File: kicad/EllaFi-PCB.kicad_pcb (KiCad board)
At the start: 2 copper layers, 43.8 x 97.2 mm, 27 parts, among them J1 Conn_01x04_Socket, J2 Conn_01x03, J3 PJ-102AH, J4 Conn_01x22_Socket, J5 Conn_01x22_Socket, Q1 AOD4184A, SW1 2W/3W jumper, U1 FOD817S, U2 ESP32-S3-DevKitC, U3 LM2596S-5

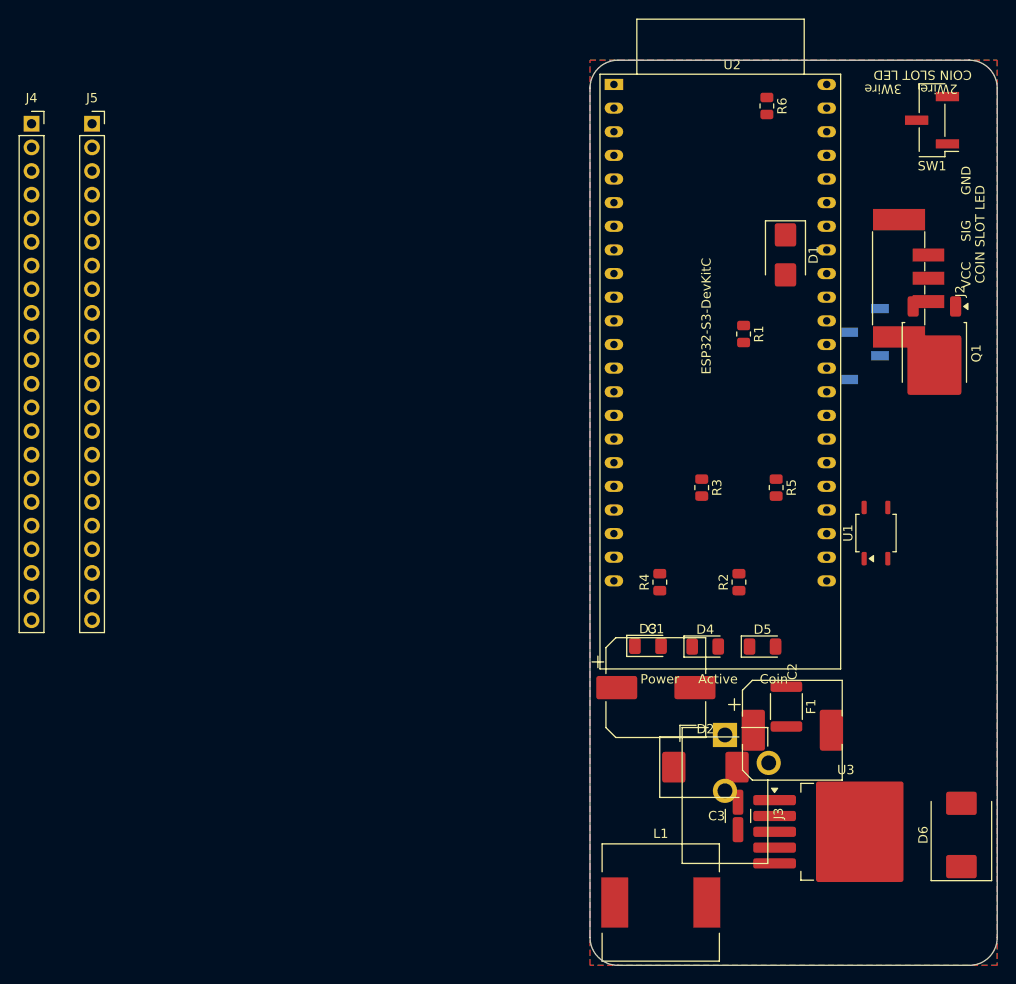
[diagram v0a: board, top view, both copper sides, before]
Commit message: kicad: PCB fully routed + DRC-clean (buck complete)
MPM3620A buck routed (FB on top layer, no via; grounds via'd to the plane), J3/F1/D6 input front-end, coin/signal nets, GND pours filled. Net-class track widths 0.25mm. DRC: 0 unconnected, 0 violations. Buck spike test passes (12.1V vs LM2596's 30.3V).

Co-Authored-By: Claude Opus 4.8 <noreply@anthropic.com>
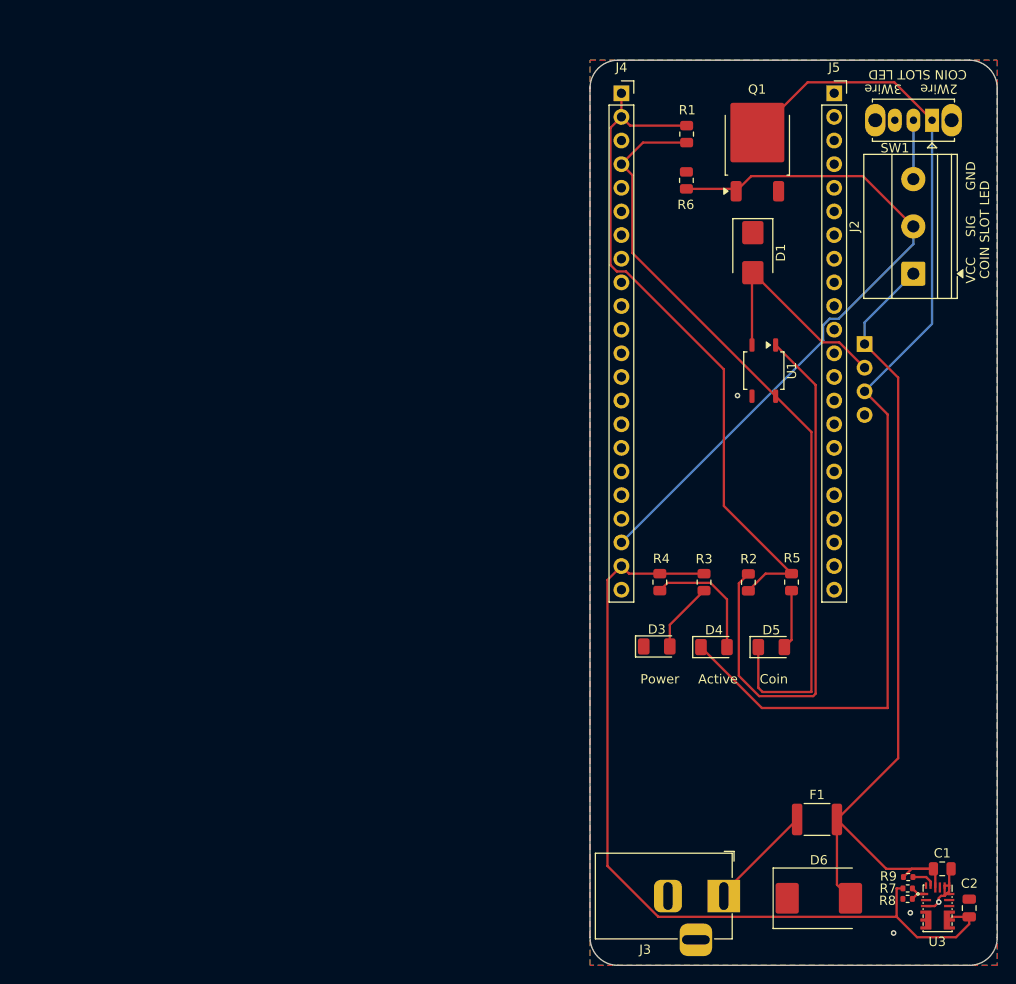
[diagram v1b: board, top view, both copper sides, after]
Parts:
- removed C3: 10uF, Capacitor_SMD:C_1210_3225Metric
- removed D2: SS54, Diode_SMD:D_SMC
- removed L1: 47uH, Inductor_SMD:L_12x12mm_H8mm
- removed U2: ESP32-S3-DevKitC, PCM_Espressif:ESP32-S3-DevKitC
- added R7: 100 kΩ, Resistor_SMD:R_0402_1005Metric, F.Cu at (132.1, 139.5)
- added R8: 19.1 kΩ, Resistor_SMD:R_0402_1005Metric, F.Cu at (132.1, 140.6)
- added R9: 100 kΩ, Resistor_SMD:R_0402_1005Metric, F.Cu at (132.2, 138.3)
- C1: value 220uF 25V -> 10 µF; footprint Capacitor_SMD:CP_Elec_10x10.5 -> Capacitor_SMD:C_0805_2012Metric
- C2: value 220uF 25V -> 22 µF; footprint Capacitor_SMD:CP_Elec_10x10.5 -> Capacitor_SMD:C_0805_2012Metric
- D3: value LED-RED -> RED
- D4: value LED-YELLOW -> YELLOW
- D5: value LED-GREEN -> GREEN
- J1: footprint Connector_PinSocket_2.54mm:PinSocket_1x04_P2.54mm_Vertical_SMD_Pin1Left -> Connector_PinSocket_2.54mm:PinSocket_1x04_P2.54mm_Vertical
- J2: footprint TerminalBlock_Phoenix:TerminalBlock_Phoenix_PTSM-0,5-3-2,5-V-SMD_1x03-1MP_P2.50mm_Vertical -> TerminalBlock_Phoenix:TerminalBlock_Phoenix_MKDS-1,5-3-5.08_1x03_P5.08mm_Horizontal
- J3: value PJ-102AH -> PJ-002AH; footprint Connector_BarrelJack:BarrelJack_CUI_PJ-102AH_Horizontal -> Connector_BarrelJack:BarrelJack_Horizontal
- SW1: value 2W/3W jumper -> OS102011MS2QN1; footprint Connector_PinHeader_2.54mm:PinHeader_1x03_P2.54mm_Vertical_SMD_Pin1Left -> Button_Switch_THT:SW_Slide_SPDT_Straight_CK_OS102011MS2Q
- U3: value LM2596S-5 -> MPM3620AGQV-Z; footprint Package_TO_SOT_SMD:TO-263-5_TabPin3 -> MPM3620A:QFN-20_L5.0-W3.0-TL-MPM3630GQV-Z
- moved J5 79.8 mm to (124.2, 54.1)
- moved J4 63.5 mm to (101.4, 54.1)
- moved C1 36.4 mm to (135.8, 137.4)
- moved Q1 29.4 mm to (116.0, 59.5), turned to 90 degrees
- moved C2 26.9 mm to (138.7, 141.6), turned to 90 degrees
- moved R1 22.3 mm to (108.4, 58.4), turned to 90 degrees
- moved U1 21.2 mm to (116.7, 83.9), turned to -90 degrees
- moved J3 17.3 mm to (112.4, 140.3)
- moved D6 16.8 mm to (122.6, 140.5), turned to 0 degrees
- moved F1 12.6 mm to (122.4, 132.1), turned to 0 degrees
- moved U3 12.5 mm to (135.4, 141.0)
- moved R6 11.8 mm to (108.4, 63.4)
- moved R5 10.3 mm to (119.7, 106.6)
- moved R3 10.2 mm to (110.3, 106.6)
- moved D1 3.52 mm to (115.5, 71.2)
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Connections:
- C2 pad 1: Net-(U2-5V) -> /5V
- D5 pad 1: Net-(D5-K) -> /GPIO4
- J2 pad 2: Net-(J2-Pin_2) -> /GPIO14
- J4 pad 1: unconnected-(J4-Pin_1-Pad1) -> /3V3
- J4 pad 2: unconnected-(J4-Pin_2-Pad2) -> /3V3
- J4 pad 20: unconnected-(J4-Pin_20-Pad20) -> /GPIO14
- J4 pad 21: unconnected-(J4-Pin_21-Pad21) -> /5V
- J4 pad 22: unconnected-(J4-Pin_22-Pad22) -> GND
- J4 pad 4: unconnected-(J4-Pin_4-Pad4) -> /GPIO4
- J5 pad 1: unconnected-(J5-Pin_1-Pad1) -> GND
- J5 pad 21: unconnected-(J5-Pin_21-Pad21) -> GND
- J5 pad 22: unconnected-(J5-Pin_22-Pad22) -> GND
- Q1 pad 1: Net-(J2-Pin_2) -> /GPIO14
- R1 pad 1: Net-(U2-GPIO4/ADC1_CH3) -> /GPIO4
- R1 pad 2: Net-(D5-K) -> /3V3
- R2 pad 1: Net-(R2-Pad1) -> /3V3
- R3 pad 1: Net-(U2-5V) -> /5V
- R4 pad 2: Net-(U2-5V) -> /5V
- R5 pad 1: Net-(R2-Pad1) -> /3V3
- R6 pad 2: Net-(J2-Pin_2) -> /GPIO14
- U1 pad 4: Net-(D5-K) -> /GPIO4
- U3 pad 1: Net-(D6-A2) -> Net-(U3-FB)
- U3 pad 2: Net-(D2-K) -> unconnected-(U3-VCC-Pad2)
- U3 pad 4: Net-(U2-5V) -> unconnected-(U3-SW-Pad4)
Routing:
- net Net-(D4-K): track 0.00 -> 112.7 mm
- net Net-(D6-A2): track 0.00 -> 92.3 mm
- net /5V: track 0.00 -> 91.5 mm
- net /GPIO4: track 0.00 -> 83.4 mm
- net /GPIO14: track 0.00 -> 74.9 mm
- net /3V3: track 0.00 -> 73.5 mm
- net Net-(R2-Pad2): track 0.00 -> 59.9 mm
- net Net-(D1-A2): track 0.00 -> 24.0 mm
- net Net-(D4-A): track 0.00 -> 13.4 mm
- net +12V: track 0.00 -> 11.5 mm
- net GND: track 0.00 -> 7.97 mm, vias 0 -> 4
- net Net-(D3-A): track 0.00 -> 7.52 mm
- net Net-(D5-A): track 0.00 -> 6.39 mm
- net Net-(J2-Pin_3): track 0.00 -> 6.33 mm
- net Net-(U3-FB): track 0.00 -> 3.07 mm
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
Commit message: kicad: whole-board validation suite + fix 4 sim-found defects
New kicad/sim/board/ (./run_all.sh): pad-polarity checker (board vs
datasheet intent), sim-sync checker (SPICE model vs fresh netlist
export), 11 ngspice scenario benches + 60-trial Monte Carlo.

Defects the suite found, fixed in schematic+PCB:
- D4 saw 7V reverse (5V-max LED) whenever Q1 off -> moved with R4 to
  the gate side; also now clamps GPIO14 during boot vs pullup panels
- reversed adapter put -12V on the buck -> D6 1.5SMC18CA (bidir) ->
  1.5SMC18A (unidir), band to 12V rail; clamps -0.8V, F1 trips
- D1 coin-line TVS installed backwards (band on GND -> would clamp
  the coin line at 0.7V; dead coin input) -> flipped
- low-CTR/aged optos left GPIO4 above the 0.825V logic-low ceiling
  (~5% of builds) -> R1 1k->2.2k, R5 220->1k (4.7k rejected: too slow
  recovering from coupled noise bursts)

globals.h: J2.2 3-wire panel TODO closed with the sim verdict; stale
IRLZ44N/10k comment facts corrected. Findings + lessons recorded in
memory/hardware_notes.md. ERC 0, DRC 0, suite ALL PASS.

Co-Authored-By: Claude Fable 5 <noreply@anthropic.com>
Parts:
- D3: value RED -> LED-RED
- D4: value YELLOW -> LED-YELLOW
- D5: value GREEN -> LED-GREEN
- D6: value 1.5SMC18CA -> 1.5SMC18A
- F1: value miniSMDC150F -> MINISMDC150F/16-2
- R1: value 1k -> 2.2k
- R5: value 220 -> 1k
- moved R4 5.33 mm to (110.8, 106.4)
- moved R3 3.87 mm to (106.4, 106.5)
- turned D1 to 90 degrees
- turned D6 to 180 degrees
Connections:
- C1 pad 1: Net-(D6-A2) -> Net-(D6-A1)
- D1 pad 1: GND -> Net-(D1-A1)
- D1 pad 2: Net-(D1-A2) -> GND
- D4 pad 2: Net-(D4-A) -> /GPIO14
- D6 pad 1: GND -> Net-(D6-A1)
- D6 pad 2: Net-(D6-A2) -> GND
- F1 pad 2: Net-(D6-A2) -> Net-(D6-A1)
- J1 pad 1: Net-(D6-A2) -> Net-(D6-A1)
- J1 pad 2: Net-(D1-A2) -> Net-(D1-A1)
- J1 pad 3: Net-(D4-K) -> Net-(J1-Pin_3)
- J2 pad 1: Net-(D6-A2) -> Net-(D6-A1)
- Q1 pad 2: Net-(D4-K) -> Net-(J1-Pin_3)
- R4 pad 1: Net-(D4-A) -> Net-(D4-K)
- R4 pad 2: /5V -> GND
- R9 pad 1: Net-(D6-A2) -> Net-(D6-A1)
- SW1 pad 1: Net-(D4-K) -> Net-(J1-Pin_3)
- U1 pad 2: Net-(D1-A2) -> Net-(D1-A1)
- U3 pad 16: Net-(D6-A2) -> Net-(D6-A1)
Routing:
- net Net-(D4-K): track 112.7 -> 6.57 mm
- net Net-(D6-A2): track 92.3 -> 0.00 mm
- net Net-(D6-A1): track 0.00 -> 92.3 mm
- net Net-(J1-Pin_3): track 0.00 -> 54.8 mm
- net Net-(D1-A2): track 24.0 -> 0.00 mm
- net Net-(D1-A1): track 0.00 -> 24.0 mm
- net /GPIO14: track 74.9 -> 96.8 mm
- net Net-(D4-A): track 13.4 -> 0.00 mm
- net /5V: track 91.5 -> 87.6 mm
- net Net-(D3-A): track 7.52 -> 6.16 mm
- net GND: vias 4 -> 5

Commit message: kicad: power tracks widened to 0.8mm (user layout pass) + GND stitching vias + D6 PCB field sync
DRC 0 violations / 0 unconnected; remaining 6 parity notes = known U3
merged-pad numbering quirk. Gate green.

Co-Authored-By: Claude Fable 5 <noreply@anthropic.com>
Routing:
- net /5V: track 87.6 -> 90.2 mm
- net Net-(D6-A1): track 92.3 -> 90.0 mm
- net Net-(J1-Pin_3): track 54.8 -> 56.7 mm
- net (no net): vias 0 -> 6
